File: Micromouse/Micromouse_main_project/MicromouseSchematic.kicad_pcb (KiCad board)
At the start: 2 copper layers, 155.7 x 48 mm, 101 parts, among them J1 Conn_01x06_MountingPin, J10 Conn_01x06_MountingPin, J11 Conn_01x07_Pin, J12 IR_1, J2 Conn_01x06_MountingPin, J3 Conn_01x03_Pin, J4 Conn_01x02_Pin, J5 Conn_01x06_MountingPin, J6 IR_1, J7 IR_1, J8 IR_1, Q1 SFH300, Q10 DMN3065LW-7, Q2 DMN3065LW-7, Q3 SFH300, Q4 DMN3065LW-7, Q5 SFH300, Q6 DMN3065LW-7, Q9 SFH300, SW1 SW_Push, SW2 SW_Push, U1 VL53L1CXV0FY1, U11 MP6550GG-Z, U3 ICM-42688-P, U4 LIS2MDLTR, U5 STM32F746VETx, U7 MP6550GG-Z, Y1 8MHz, Y2 32.768kHz

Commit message: Prepped layout
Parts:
- removed C26, C27, C29, C30: 100n, Capacitor_SMD:C_0402_1005Metric
- removed C28, C31: 6.8p, Capacitor_SMD:C_0402_1005Metric
- removed C32: 10u, Capacitor_SMD:C_0402_1005Metric
- removed C33, C35: 1u, Capacitor_SMD:C_0402_1005Metric
- removed C34: 10n, Capacitor_SMD:C_0402_1005Metric
- removed C36, C37: 0.47 μF, Capacitor_SMD:C_0402_1005Metric
- removed C38: 0.1 μF, Capacitor_SMD:C_0402_1005Metric
- removed C39: 2.2 μF, Capacitor_SMD:C_0402_1005Metric
- removed C40: 10 nF, Capacitor_SMD:C_0402_1005Metric
- removed D1, D2, D3, D5: SFH4550, LED_THT:LED_D5.0mm_IRGrey
- removed Q1, Q3, Q5, Q9: SFH300, LED_THT:LED_D5.0mm_Clear
- removed Q10, Q2, Q4, Q6: DMN3065LW-7, MM_DMN3065LW-7:DMN3065LW-7
- removed R20: 10k, Resistor_SMD:R_0603_1608Metric
- removed R21, R22: 5 kΩ, Resistor_SMD:R_0805_2012Metric
- removed R23, R24, R26, R27, R35, R36, R37, R38, R39, R40, R41, R42: 10 kΩ, Resistor_SMD:R_0603_1608Metric
- removed U11, U7: MP6550GG-Z, MM_MP6550G-Z:MP6550_MNP
- removed U5: STM32F746VETx, Package_QFP:LQFP-100_14x14mm_P0.5mm
- added C14: 10u, Capacitor_SMD:C_0603_1608Metric, F.Cu at (213.5, 100.3)
- added C15: 1u, Capacitor_SMD:C_0603_1608Metric, F.Cu at (146.5, 78.0)
- added C16: 10n, Capacitor_SMD:C_0603_1608Metric, F.Cu at (152.0, 73.7)
- added C17: 1u, Capacitor_SMD:C_0603_1608Metric, F.Cu at (150.0, 73.7)
- added C18: 0.47u, Capacitor_SMD:C_0603_1608Metric, F.Cu at (143.8, 117.5)
- added Cin_MD2: 22u, Capacitor_SMD:C_0603_1608Metric, F.Cu at (162.7, 120.8)
- added J13: IR_2, Connector_PinHeader_2.00mm:PinHeader_1x04_P2.00mm_Vertical, F.Cu at (109.0, 52.0)
- added J14: IR_4, Connector_PinHeader_2.00mm:PinHeader_1x04_P2.00mm_Vertical, F.Cu at (205.0, 53.0)
- added J15: Conn_01x07_Pin, Connector_PinSocket_2.54mm:PinSocket_1x07_P2.54mm_Vertical, F.Cu at (148.9, 53.5)
- added J9: Conn_01x06_MountingPin, Connector_JST:JST_SH_BM06B-SRSS-TB_1x06-1MP_P1.00mm_Vertical, F.Cu at (128.0, 140.8)
- added R13: 10k, Resistor_SMD:R_0603_1608Metric, F.Cu at (165.0, 123.5)
- added U2: MP6550GG-Z, footprints:IC12_MP6550_MNP, F.Cu at (147.5, 121.0)
- C1: value 0.47 μF -> 27p; footprint Capacitor_SMD:C_0201_0603Metric -> Capacitor_SMD:C_0603_1608Metric
- C10, C12, C13, C8: value 1uF -> 100n; footprint Capacitor_SMD:C_0402_1005Metric -> Capacitor_SMD:C_0603_1608Metric
- C11: value 100nF -> 100n; footprint Capacitor_SMD:C_0402_1005Metric -> Capacitor_SMD:C_0603_1608Metric
- C19: value 0.1u -> 0.47u; footprint Capacitor_SMD:C_0402_1005Metric -> Capacitor_SMD:C_0603_1608Metric
- C2: value 22 µF -> 100n; footprint Capacitor_SMD:C_0402_1005Metric -> Capacitor_SMD:C_0603_1608Metric
- C20, C21: value 10p -> 0.47u; footprint Capacitor_SMD:C_0402_1005Metric -> Capacitor_SMD:C_0603_1608Metric
- C22: value 2.2u -> 22u; footprint Capacitor_SMD:C_0402_1005Metric -> Capacitor_SMD:C_0603_1608Metric
- C23: value 2.2u -> 10n; footprint Capacitor_SMD:C_0402_1005Metric -> Capacitor_SMD:C_0603_1608Metric
- C24: footprint Capacitor_SMD:C_0402_1005Metric -> Capacitor_SMD:C_0603_1608Metric
- C25: value 100n -> 2.2u; footprint Capacitor_SMD:C_0402_1005Metric -> Capacitor_SMD:C_0603_1608Metric
- C3: value 0.47 μF -> 27p; footprint Capacitor_SMD:C_0402_1005Metric -> Capacitor_SMD:C_0603_1608Metric
- C4: value 220 nF -> 2.2u; footprint Capacitor_SMD:C_0402_1005Metric -> Capacitor_SMD:C_0603_1608Metric
- C5: value 100 nF -> 2.2u; footprint Capacitor_SMD:C_0402_1005Metric -> Capacitor_SMD:C_0603_1608Metric
- C6: value 100 nF -> 15p; footprint Capacitor_SMD:C_0402_1005Metric -> Capacitor_SMD:C_0603_1608Metric
- C7: value 10 μF -> 15p; footprint Capacitor_SMD:C_0402_1005Metric -> Capacitor_SMD:C_0603_1608Metric
- C9: value 4.7uF -> 100n; footprint Capacitor_SMD:C_0402_1005Metric -> Capacitor_SMD:C_0603_1608Metric
- Cin_MD1: value 22 μF -> 22u; footprint Capacitor_SMD:C_0402_1005Metric -> Capacitor_SMD:C_0603_1608Metric
- Cin_VR1: value 10 µF -> 10u; footprint Capacitor_SMD:C_0402_1005Metric -> Capacitor_SMD:C_0603_1608Metric
- FB1: value FerriteBead -> 120R; footprint Resistor_SMD:R_0805_2012Metric -> Inductor_SMD:L_0603_1608Metric
- J1: value Conn_01x06_MountingPin -> Conn_01x02_Pin; footprint Connector_JST:JST_PH_B6B-PH-K_1x06_P2.00mm_Vertical -> Connector_JST:JST_PH_B2B-PH-K_1x02_P2.00mm_Vertical
- J10: footprint Connector_JST:JST_ZH_B6B-ZR_1x06_P1.50mm_Vertical -> Connector_JST:JST_SH_BM06B-SRSS-TB_1x06-1MP_P1.00mm_Vertical
- J11: value Conn_01x07_Pin -> IR_1; footprint Connector_JST:JST_ZH_B7B-ZR_1x07_P1.50mm_Vertical -> Connector_PinHeader_2.00mm:PinHeader_1x04_P2.00mm_Vertical
- J12: value IR_1 -> IR_3; footprint Connector_JST:JST_ZH_B4B-ZR_1x04_P1.50mm_Vertical -> Connector_PinHeader_2.00mm:PinHeader_1x04_P2.00mm_Vertical
- J2: footprint Connector_JST:JST_PH_B6B-PH-K_1x06_P2.00mm_Vertical -> Connector_PinHeader_2.54mm:PinHeader_1x06_P2.54mm_Vertical
- J3: value Conn_01x03_Pin -> Conn_01x06_MountingPin; footprint Connector_JST:JST_ZH_B3B-ZR_1x03_P1.50mm_Vertical -> Connector_PinSocket_2.54mm:PinSocket_1x06_P2.54mm_Vertical
- J4: value Conn_01x02_Pin -> Conn_01x06_Pin; footprint Connector_JST:JST_PH_B2B-PH-K_1x02_P2.00mm_Vertical -> Connector_PinHeader_2.00mm:PinHeader_1x06_P2.00mm_Vertical
- J5: value Conn_01x06_MountingPin -> Conn_01x06_Pin; footprint Connector_JST:JST_ZH_B6B-ZR_1x06_P1.50mm_Vertical -> Connector_PinHeader_2.00mm:PinHeader_1x06_P2.00mm_Vertical
- J6: value IR_1 -> Conn_01x06_Pin; footprint Connector_JST:JST_ZH_B4B-ZR_1x04_P1.50mm_Vertical -> Connector_PinHeader_2.00mm:PinHeader_1x06_P2.00mm_Vertical
- J7, J8: value IR_1 -> Conn_01x01_Pin; footprint Connector_JST:JST_ZH_B4B-ZR_1x04_P1.50mm_Vertical -> Connector_PinHeader_2.54mm:PinHeader_1x01_P2.54mm_Vertical
- R10, R12, R6: value 100 -> 10k
- R2, R3: value 10k -> 3.3k
- R8: value 100 -> 5k
- R9: value 10k -> 5k
- SW1, SW2: footprint Button_Switch_THT:SW_SPST_Omron_B3F-40xx -> Button_Switch_SMD:SW_SPST_SKQG_WithStem
- U1: value VL53L1CXV0FY1 -> STM32F746VETx; footprint MM_VL53L4CDV0DH-1:LGA12_STM -> Package_QFP:LQFP-100_14x14mm_P0.5mm
- U3: value ICM-42688-P -> MP6550GG-Z; footprint MM_ICM_42688_P:ICM_42688_P -> footprints:IC12_MP6550_MNP
- U4: value LIS2MDLTR -> ICM-42688-P; footprint MM_LIS2MDLTR:LIS2MDLTR -> ICM_42688_P_FOOTPRINT:ICM_42688_P
- VR1: footprint MM_TPSM861253RDXR:TPSM861253RDXR -> TPSM862253RDXR_FOOTPRINT:TPSM861253RDXR
- moved Renb1 143.1 mm to (162.8, 136.5), turned to 0 degrees
- moved Rent1 142.5 mm to (162.8, 139.0), turned to 0 degrees
- moved Cin_VR1 137.1 mm to (150.8, 138.5), turned to 0 degrees
- moved J5 136.1 mm to (151.5, 33.0), turned to 90 degrees
- moved VR1 134.6 mm to (156.5, 139.2), turned to 0 degrees
- moved C9 127.4 mm to (213.5, 87.7)
- moved FB1 126.0 mm to (147.0, 75.0)
- moved C11 125.7 mm to (213.5, 92.8)
- moved J8 122.9 mm to (120.5, 141.2), turned to 0 degrees
- moved R1 116.5 mm to (170.0, 56.5), turned to 180 degrees
- moved Y2 116.4 mm to (160.5, 69.5), turned to 90 degrees
- moved Y1 116.4 mm to (156.5, 68.4), turned to -90 degrees
- moved J2 113.2 mm to (162.8, 48.5), turned to -90 degrees
- moved C10 110.1 mm to (213.5, 90.2)
- moved J3 107.3 mm to (174.5, 78.8)
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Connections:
- C1 pad 1: +3.3V -> GND
- C1 pad 2: GND -> Net-(U1-PH0)
- C10 pad 1: Net-(D1-A) -> +3.3V
- C12 pad 1: Net-(D2-A) -> +3.3V
- C13 pad 1: Net-(D3-A) -> +3.3V
- C19 pad 1: NRST -> Net-(U3-VCC)
- C2 pad 1: +3.3V -> NRST
- C20 pad 1: Net-(U5-PH0) -> Net-(J8-Pin_1)
- C20 pad 2: Net-(C20-Pad2) -> GND
- C21 pad 1: Net-(C21-Pad1) -> Net-(J7-Pin_1)
- C21 pad 2: Net-(U5-PH1) -> GND
- C22 pad 1: Net-(U5-VCAP_1) -> +3.3V
- C23 pad 1: Net-(U5-VCAP_2) -> +3.3V
- C3 pad 1: Net-(U7-VCC) -> GND
- C3 pad 2: GND -> Net-(U1-PH1)
- C4 pad 1: Net-(U4-C1) -> Net-(U1-VCAP_1)
- C5 pad 1: +3.3V -> Net-(U1-VCAP_2)
- C6 pad 1: +3.3V -> Net-(U1-PC15)
- C7 pad 1: +3.3V -> Net-(U1-PC14)
- C8 pad 1: Net-(D5-A) -> +3.3V
- J1 pad 1: Net-(J1-Pin_1) -> +7.4V
- J1 pad 2: Net-(J1-Pin_2) -> GND
- J10 pad 1: +3.3V -> Net-(J10-Pin_1)
- J10 pad 2: SWDIO -> Net-(J10-Pin_2)
- J10 pad 3: SWCLK -> +3.3V
- J10 pad 4: GND -> Encoder_A_1
- J10 pad 5: NRST -> Encoder_B_1
- J10 pad 6: SWO -> GND
- J11 pad 1: +3.3V -> GND
- J11 pad 2: I2C_SCL -> IR_REC_1
- J11 pad 3: I2C_SDA -> IR_POW_1
- J11 pad 4: IMU_INT_1 -> +3.3V
- J12 pad 1: +3.3V -> GND
- J12 pad 2: IR_POW_1 -> IR_REC_3
- J12 pad 3: IR_REC_1 -> IR_POW_3
- J12 pad 4: GND -> +3.3V
- J2 pad 1: Net-(J2-Pin_1) -> +3.3V
- J2 pad 2: Net-(J2-Pin_2) -> SWDIO
- J2 pad 3: +3.3V -> SWCLK
- J2 pad 4: Encoder_A_2 -> GND
- J2 pad 5: Encoder_B_2 -> NRST
- J2 pad 6: GND -> SWO
- J3 pad 1: +3.3V -> KEY
- J3 pad 2: GND -> +3.3V
- J3 pad 3: +7.4V -> GND
- J4 pad 1: +7.4V -> GND
- J4 pad 2: GND -> TOF_SHUT1
- J5 pad 1: KEY -> GND
- J5 pad 2: +3.3V -> TOF_SHUT2
- J5 pad 3: GND -> I2C_SCL
- J5 pad 4: TXD -> I2C_SDA
- J5 pad 5: RXD -> TOF_INT2
- J5 pad 6: STATE -> +3.3V
- J6 pad 1: +3.3V -> GND
- J6 pad 2: IR_POW_2 -> TOF_SHUT3
- J6 pad 3: IR_REC_2 -> I2C_SCL
- J6 pad 4: GND -> I2C_SDA
- J7 pad 1: +3.3V -> Net-(J7-Pin_1)
- J8 pad 1: +3.3V -> Net-(J8-Pin_1)
- R1 pad 1: +3.3V -> GND
- R1 pad 2: I2C_SCL -> Net-(U1-BOOT0)
- R10 pad 1: Net-(D2-K) -> NSLEEP_HB_2
- R10 pad 2: GND -> Net-(U2-NSLEEP_HB)
- R11 pad 1: IR_REC_4 -> Net-(U3-NSLEEP_HB)
- R11 pad 2: GND -> NSLEEP_HB_1
- R12 pad 1: Net-(D3-K) -> MO2_IN2
- R12 pad 2: GND -> Net-(U2-IN2)
- R2 pad 2: I2C_SDA -> I2C_SCL
- R3 pad 2: TOF_INT -> I2C_SDA
- R4 pad 1: +3.3V -> Net-(U3-NSLEEP_LDO)
- R4 pad 2: TOF_CE -> NSLEEP_LDO_1
- R5 pad 1: IR_REC_1 -> Net-(U2-NSLEEP_LDO)
- R5 pad 2: GND -> NSLEEP_LDO_2
- R6 pad 2: GND -> MO2_IN1
- R7 pad 1: IR_REC_2 -> Net-(U3-IN1)
- R7 pad 2: GND -> MO1_IN1
- R9 pad 1: IR_REC_3 -> Net-(U3-ISET)
- SW2 pad 1: Net-(U5-BOOT0) -> Net-(U1-BOOT0)
- U1 pad 1: +3.3V -> IR_POW_1
- U1 pad 10: I2C_SCL -> GND
- U1 pad 12: GND -> Net-(U1-PH0)
- U1 pad 2: GND -> IR_POW_2
- U1 pad 3: GND -> IR_POW_3
- U1 pad 4: GND -> IR_POW_4
- U1 pad 5: TOF_CE -> unconnected-(U1-PE6-Pad5)
- U1 pad 6: GND -> +3.3V
- U1 pad 7: TOF_INT -> unconnected-(U1-PC13-Pad7)
- U1 pad 8: unconnected-(U1-DNC-Pad8) -> Net-(U1-PC14)
- U1 pad 9: I2C_SDA -> Net-(U1-PC15)
- U3 pad 1: GND -> Net-(U3-IN1)
- U3 pad 10: unconnected-(U3-RESV_10-Pad10) -> Net-(U3-IN2)
- U3 pad 11: GND -> VISEN_1
- U3 pad 12: +3.3V -> Net-(U3-NSLEEP_HB)
- U3 pad 2: unconnected-(U3-RESV_2-Pad2) -> Net-(J10-Pin_1)
- U3 pad 3: unconnected-(U3-RESV_3-Pad3) -> GND
- U3 pad 4: IMU_INT_1 -> Net-(J7-Pin_1)
- U3 pad 5: +3.3V -> Net-(U3-NSLEEP_LDO)
- U3 pad 6: GND -> Net-(U3-VCC)
- U3 pad 7: GND -> Net-(U3-ISET)
- U3 pad 8: +3.3V -> Net-(J10-Pin_2)
- U3 pad 9: IMU_INT_2 -> +7.4V
- U4 pad 1: I2C_SCL -> IMU_MISO
- U4 pad 10: +3.3V -> unconnected-(U4-RESV_10-Pad10)
- U4 pad 11: unconnected-(U4-NC2-Pad11) -> GND
- U4 pad 12: unconnected-(U4-NC3-Pad12) -> IMU_CS
- U4 pad 3: +3.3V -> unconnected-(U4-RESV_3-Pad3)
- U4 pad 4: I2C_SDA -> IMU_INT_1
- U4 pad 5: Net-(U4-C1) -> +3.3V
- U4 pad 7: MAG_INT -> GND
- U4 pad 8: GND -> +3.3V
- U4 pad 9: +3.3V -> IMU_INT_2
- Y1 pad 1: Net-(C20-Pad2) -> Net-(U1-PH0)
- Y1 pad 2: Net-(C21-Pad1) -> Net-(U1-PH1)
- Y2 pad 1: Net-(C28-Pad2) -> Net-(U1-PC15)
- Y2 pad 2: Net-(C31-Pad2) -> Net-(U1-PC14)
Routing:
- net GND: track 183.2 -> 0.00 mm, vias 12 -> 0
- net +3.3V: track 148.5 -> 0.00 mm
- net +7.4V: track 30.3 -> 0.00 mm
- net IR_REC_2: track 20.2 -> 0.00 mm
- net IR_REC_1: track 19.9 -> 0.00 mm
- net IR_REC_3: track 19.8 -> 0.00 mm
- net IR_REC_4: track 19.8 -> 0.00 mm
- net I2C_SDA: track 10.5 -> 0.00 mm
- net Net-(D2-A): track 9.14 -> 0.00 mm
- net Net-(D3-A): track 9.10 -> 0.00 mm
- net Net-(D5-A): track 9.07 -> 0.00 mm
- net Net-(D1-A): track 8.95 -> 0.00 mm
- net I2C_SCL: track 8.65 -> 0.00 mm
- net Net-(U2-IN1): track 7.84 -> 0.00 mm
- net Net-(U2-ISET): track 7.33 -> 0.00 mm
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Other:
- board size 155.7 x 48 mm -> 114.8 x 115 mm
- board text removed: "Base board"
- board text removed: "IMU&Mag"
- board text removed: "Motor Drivers"
- board text removed: "ToF"
- board text removed: "Voltage regulator"

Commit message: Finished layout
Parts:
- removed the C20 at (149.2, 117.5)
- removed the C21 at (171.2, 119.5)
- removed the J7 at (193.0, 141.0)
- removed the J8 at (120.5, 141.2)
- removed the R4 at (167.0, 116.5)
- removed the R5 at (147.0, 117.4)
- moved C10 69.2 mm to (145.2, 79.0), turned to 180 degrees
- moved C11 66.5 mm to (147.0, 93.0), turned to 180 degrees
- moved C13 61.4 mm to (158.2, 71.0), turned to 90 degrees
- moved C9 59.7 mm to (156.2, 71.0), turned to 90 degrees
- moved J7 55.5 mm to (183.5, 140.5), turned to 0 degrees
- moved J8 55.5 mm to (128.0, 140.8), turned to 0 degrees
- moved C14 49.1 mm to (164.6, 96.8)
- moved C12 49.0 mm to (164.5, 94.8)
- moved C8 46.7 mm to (167.5, 76.2)
- moved C19 27.1 mm to (143.2, 125.0), turned to -90 degrees
- moved J1 26.8 mm to (169.2, 138.0), turned to 90 degrees
- moved R5 24.2 mm to (147.8, 115.9), turned to 90 degrees
- moved R10 23.7 mm to (170.0, 121.5), turned to 180 degrees
- moved Cin_MD1 22.9 mm to (166.5, 124.2), turned to -90 degrees
- moved R8 21.2 mm to (169.9, 119.0)
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- renumbered C22 to C20, C23 to C21, C24 to C22, C25 to C23, J11 to J10, J12 to J11, J13 to J12, J14 to J13, J9 to J7, J10 to J8, J15 to J9, R12 to R10, R13 to R11, R6 to R4, R7 to R5, R8 to R6, R9 to R7, R10 to R8, R11 to R9
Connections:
- U1 pad 38: NSLEEP_LDO_1 -> unconnected-(U1-PE8-Pad38)
- U1 pad 42: NSLEEP_LDO_2 -> unconnected-(U1-PE12-Pad42)
- U2 pad 4: Net-(J8-Pin_1) (its old number) -> unconnected-(U2-V3P3-Pad4)
- U2 pad 5: Net-(U2-NSLEEP_LDO) -> unconnected-(U2-NSLEEP_LDO-Pad5)
- U3 pad 4: Net-(J7-Pin_1) (its old number) -> unconnected-(U3-V3P3-Pad4)
- U3 pad 5: Net-(U3-NSLEEP_LDO) -> unconnected-(U3-NSLEEP_LDO-Pad5)
- VR1 pad 14: (no net) -> +3.3V
- VR1 pad 15: (no net) -> +3.3V
- VR1 pad 16: (no net) -> +3.3V
- VR1 pad 17: (no net) -> +3.3V
- VR1 pad 18: (no net) -> +3.3V
- VR1 pad 19: (no net) -> +3.3V
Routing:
- net +3.3V: track 0.00 -> 566.5 mm, vias 0 -> 5
- net Encoder_A_2: track 0.00 -> 114.0 mm, vias 0 -> 2
- net Encoder_B_2: track 0.00 -> 112.4 mm, vias 0 -> 4
- net I2C_SCL: track 0.00 -> 93.0 mm, vias 0 -> 1
- net TOF_SHUT3: track 0.00 -> 91.9 mm, vias 0 -> 4
- net I2C_SDA: track 0.00 -> 81.8 mm, vias 0 -> 1
- net TOF_SHUT2: track 0.00 -> 76.7 mm, vias 0 -> 2
- net Encoder_A_1: track 0.00 -> 74.4 mm, vias 0 -> 2
- net Encoder_B_1: track 0.00 -> 72.0 mm, vias 0 -> 2
- net TOF_SHUT1: track 0.00 -> 71.9 mm, vias 0 -> 2
- net TOF_INT1: track 0.00 -> 71.2 mm, vias 0 -> 3
- net TOF_INT2: track 0.00 -> 69.9 mm, vias 0 -> 2
- net +7.4V: track 0.00 -> 68.9 mm, vias 0 -> 1
- net IR_POW_1: track 0.00 -> 68.0 mm, vias 0 -> 1
- net IR_POW_2: track 0.00 -> 66.5 mm, vias 0 -> 2
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- added copper zone on B.Cu, net +3.3V
- added copper zone on F.Cu, net +3.3V
- added copper zone on B.Cu, net +7.4V
- added copper zone on F.Cu, net +7.4V
- added copper zone on B.Cu, net GND
- added copper zone on F.Cu, net GND

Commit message: Cleaned up layout
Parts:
- moved C2 17.8 mm to (142.6, 56.9), turned to 180 degrees
- moved C9 5.94 mm to (162.0, 72.6)
- moved Y1 3.48 mm to (154.3, 68.2), turned to 180 degrees
- moved C1 3.11 mm to (155.6, 64.3), turned to -90 degrees
- moved C6 2.67 mm to (160.1, 66.0), turned to 90 degrees
- moved Y2 2.61 mm to (161.3, 69.1), turned to 180 degrees
- moved C3 1.94 mm to (151.9, 64.2), turned to -90 degrees
- moved C13 1.56 mm to (156.7, 71.3), turned to 180 degrees
- moved C7 1.16 mm to (162.6, 66.0)
- moved C16 0.99 mm to (151.4, 74.2)
- moved C17 0.99 mm to (149.6, 74.2)
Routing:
- net Net-(U1-PH0): track 21.3 -> 13.8 mm
- net Net-(U1-PC15): track 15.7 -> 11.0 mm
- net GND: track 6.98 -> 2.42 mm, vias 31 -> 69
- net +3.3V: track 566.5 -> 568.9 mm
- net +7.4V: track 68.9 -> 70.7 mm
- net STATE: track 16.7 -> 15.1 mm
- net TOF_INT1: track 71.2 -> 72.6 mm
- net NRST: track 47.3 -> 45.8 mm
- net SWO: track 63.2 -> 61.7 mm
- net Net-(U1-PH1): track 15.6 -> 14.2 mm
- net MAG_INT: track 47.9 -> 48.9 mm
- net IR_POW_4: track 54.8 -> 53.8 mm
- net Net-(U1-PC14): track 12.7 -> 11.9 mm
- net IR_POW_3: track 55.8 -> 55.0 mm
- net I2C_SDA: track 81.8 -> 82.6 mm
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
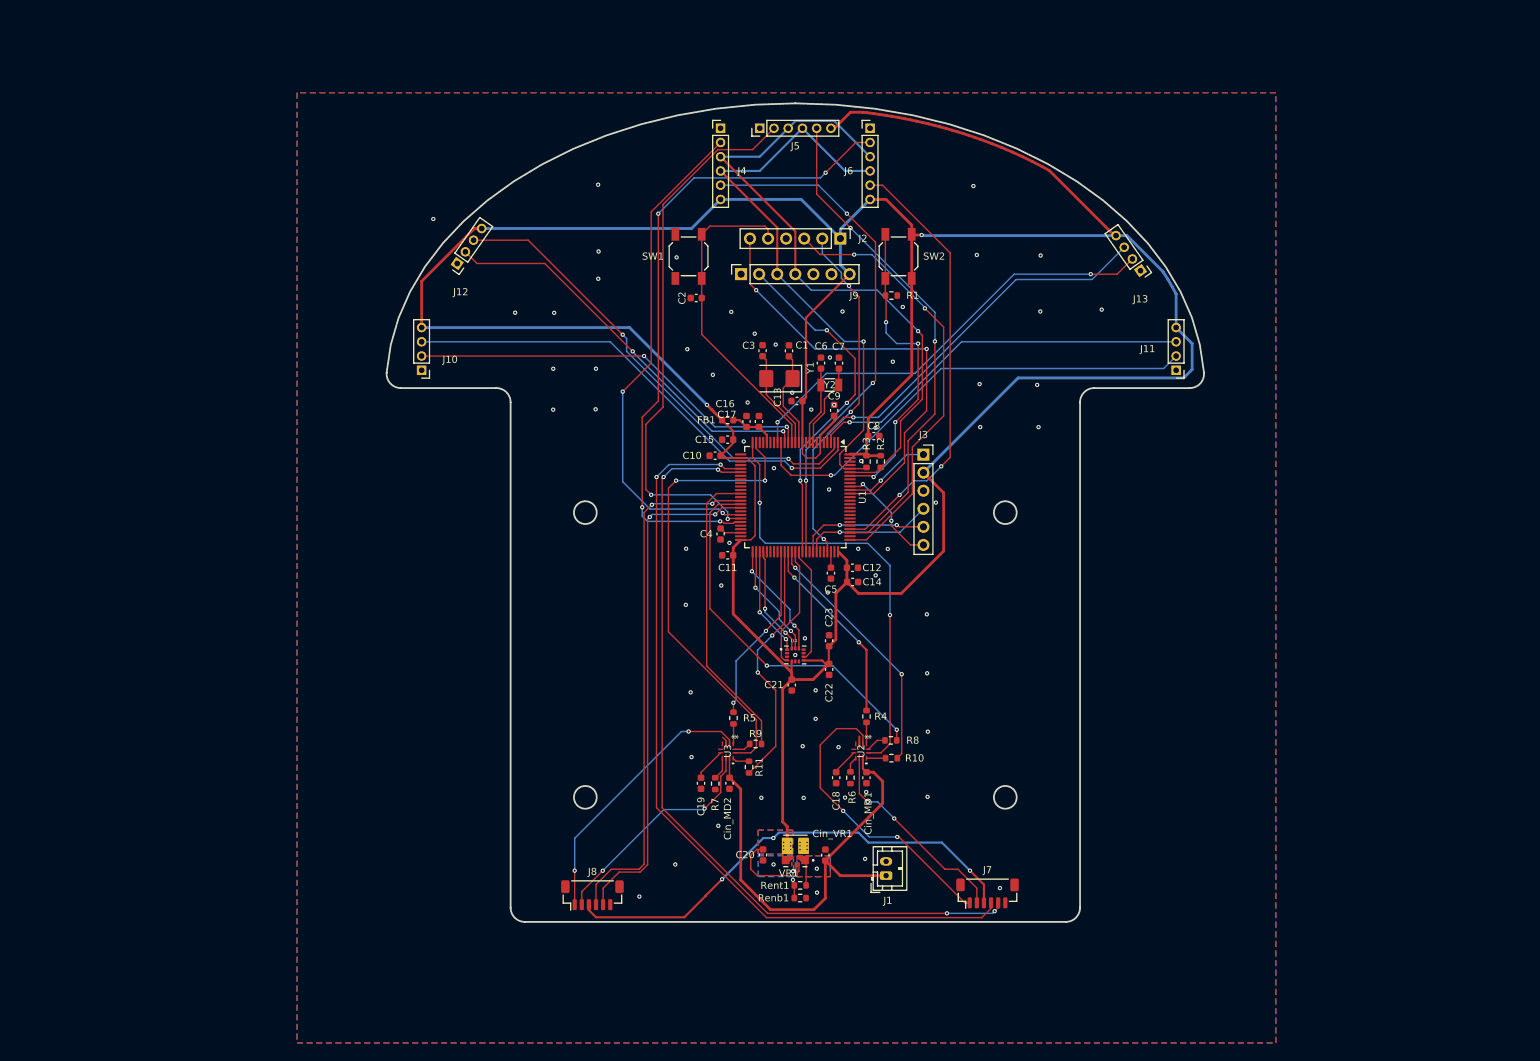
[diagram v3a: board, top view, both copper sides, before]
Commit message: Completed IR board, ToF board, changed IMU
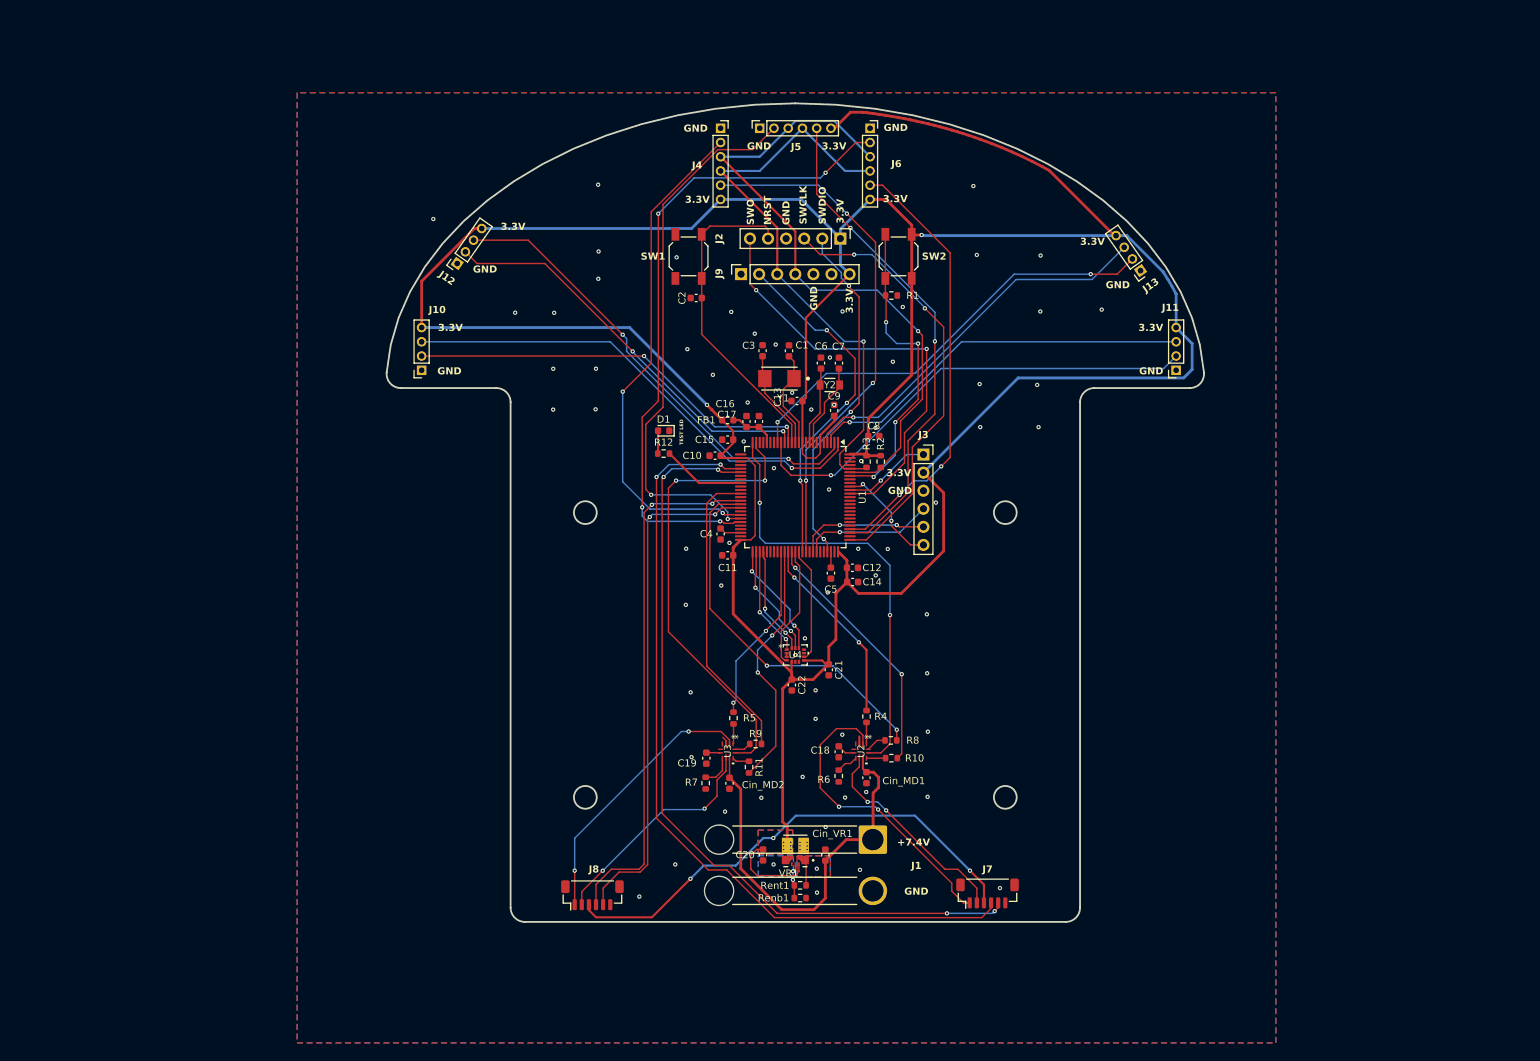
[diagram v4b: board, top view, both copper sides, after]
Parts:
- removed C23: 2.2u, Capacitor_SMD:C_0603_1608Metric
- added D1: LED, LED_SMD:LED_0603_1608Metric, F.Cu at (138.0, 75.5)
- added R12: 330, Resistor_SMD:R_0603_1608Metric, F.Cu at (138.0, 78.7)
- C21: value 10n -> 100n
- J1: footprint Connector_JST:JST_PH_B2B-PH-K_1x02_P2.00mm_Vertical -> Connector_Wire:SolderWire-2.5sqmm_1x02_P7.2mm_D2.4mm_OD3.6mm_Relief
- J10, J11, J12, J13: footprint Connector_PinHeader_2.00mm:PinHeader_1x04_P2.00mm_Vertical -> Connector_PinSocket_2.00mm:PinSocket_1x04_P2.00mm_Vertical
- J4, J5, J6: footprint Connector_PinHeader_2.00mm:PinHeader_1x06_P2.00mm_Vertical -> Connector_PinSocket_2.00mm:PinSocket_1x06_P2.00mm_Vertical
- U4: value ICM-42688-P -> LSM6DSOTR; footprint ICM_42688_P_FOOTPRINT:ICM_42688_P -> MM_LSM6DSOTR:LGA-14L_2P5X3X0P86_STM
- Y1: footprint Crystal:Crystal_SMD_5032-2Pin_5.0x3.2mm -> MM_8MHz:XTAL_ECS-80-18-30-JGN-TR
- Y2: footprint Crystal:Crystal_SMD_3215-2Pin_3.2x1.5mm -> MM_32.7kHz:XTAL_ECS-31B_ECS
- moved C22 5.68 mm to (156.0, 111.2)
- moved C21 5.62 mm to (161.2, 109.1)
- moved J1 5.39 mm to (167.4, 132.9), turned to -90 degrees
- moved C18 3.66 mm to (162.6, 120.6)
- moved C19 3.60 mm to (144.0, 121.5)
- moved R6 1.66 mm to (162.6, 124.0)
- moved R7 1.35 mm to (143.9, 125.0)
- turned Y2 to 0 degrees
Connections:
- U1 pad 34: unconnected-(U1-PB0-Pad34) -> TEST_LED
- U4 pad 11: GND -> unconnected-(U4-SDO_Aux-Pad11)
- U4 pad 2: unconnected-(U4-RESV_2-Pad2) -> GND
- U4 pad 3: unconnected-(U4-RESV_3-Pad3) -> GND
- VR1 pad 10: (no net) -> unconnected-(VR1-SW-Pad2)
- VR1 pad 11: (no net) -> unconnected-(VR1-SW-Pad2)
- VR1 pad 12: (no net) -> unconnected-(VR1-SW-Pad2)
- VR1 pad 13: (no net) -> unconnected-(VR1-SW-Pad2)
- VR1 pad 8: (no net) -> unconnected-(VR1-SW-Pad2)
- VR1 pad 9: (no net) -> unconnected-(VR1-SW-Pad2)
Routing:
- net TEST_LED: track 0.00 -> 11.7 mm
- net +7.4V: track 70.7 -> 62.1 mm
- net Net-(D1-A): track 0.00 -> 3.22 mm
- net Net-(U3-VCC): track 4.64 -> 2.01 mm
- net +3.3V: track 568.9 -> 570.9 mm
- net Net-(U3-ISET): track 3.16 -> 4.48 mm
- net Net-(J7-Pin_1): track 42.4 -> 43.7 mm
- net Net-(U2-VCC): track 3.75 -> 2.52 mm
- net Encoder_A_2: track 114.0 -> 114.8 mm
- net Net-(U2-ISET): track 2.22 -> 3.08 mm
- net Net-(J7-Pin_2): track 29.2 -> 30.0 mm
- net GND: track 2.42 -> 2.92 mm
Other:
- board text added: "+7.4V"
- board text added: "3.3V"
- board text added: "GND"
- board text added: "NRST"
- board text added: "SWCLK"
- board text added: "SWDIO"
- board text added: "SWO"
- board text added: "TEST LED"
